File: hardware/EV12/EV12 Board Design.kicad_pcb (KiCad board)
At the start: 4 copper layers, 66 x 99.3 mm, 129 parts, among them CN2 Conn_05x02_Female, CN3 Conn_01x06_Female, CN4 Conn_01x06_Female, CN5 Conn_02x05_Male, CN6 Conn_02x05_Male, CN7 Conn_02x05_Male, J1 Conn_01x02_Socket, J10 Conn_01x08_Socket, J2 AudioJack1, J3 Conn_01x06_Socket, J9 USB_C_Receptacle, SW1 TS-1037-A11B3-D2, SW3 TS-1037-A11B3-D2, SW4 SW_Push, SW5 SW_Push, SW6 SW_SPDT, U1 STM32F405RGTx, U11 ESP32-S3-WROOM-1-N8R2, U13 BM14B(0.8)-24DS-0.4V(53), U2 BQ21040DBV, U3 CH340C, U4 USBLC6-2P6, U5 M24C02-RMN6TP, U6 WM8960CGEFL/RV, U7 TPS63060, U8 STM32F072CBTx, Y1 Crystal_GND24

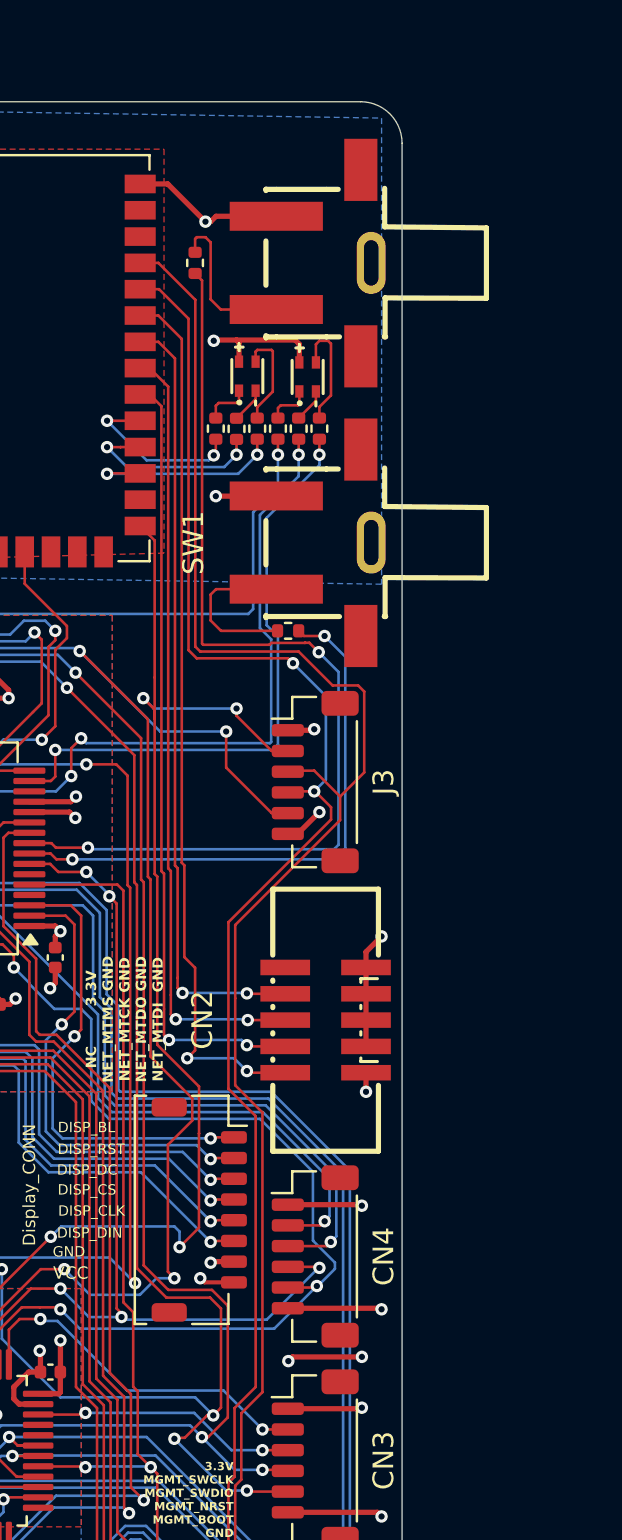
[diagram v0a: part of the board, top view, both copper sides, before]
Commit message: Replaced side buttons, switched Cap, switched to new connectors
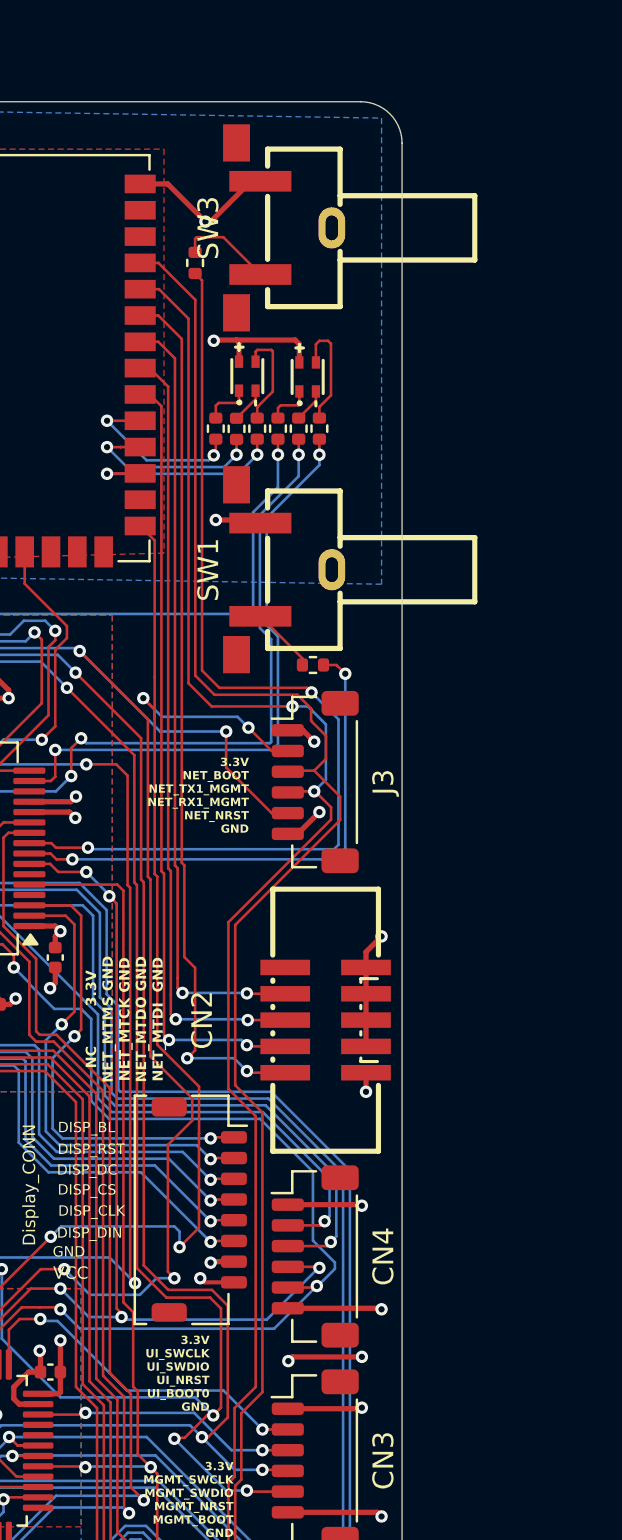
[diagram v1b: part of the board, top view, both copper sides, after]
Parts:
- SW1, SW3: footprint Hactar_Footprints:KEY-SMD_2P-L7.1-W10.6-P4.00-LS9.0 -> Hactar_Footprints:SW-SMD_L7.5-W8.0-P4.50_TS-1045-A13B3-D2
- moved SW3 2.56 mm to (174.3, 52.1)
- moved SW1 2.31 mm to (174.3, 68.6)
- moved R28 2.04 mm to (175.7, 73.2)
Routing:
- net /PTT_BTN: track 7.96 -> 3.19 mm
- net /NET_TX1_MGMT: track 100.0 -> 96.5 mm
- net /PTT_AI_BTN: track 7.66 -> 4.59 mm
- net GND: track 618.5 -> 615.7 mm
- net Net-(U1-PC0): track 27.7 -> 25.3 mm
- net Net-(U1-PC1): track 48.7 -> 48.1 mm
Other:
- board text added: "3.3V NET_BOOT NET_TX1_MGMT NET_RX1_MGMT NET_NRST GND"
- board text added: "3.3V UI_SWCLK UI_SWDIO UI_NRST UI_BOOT0 GND"

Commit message: Updated Version with fixes
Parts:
- removed SW3: TS-1037-A11B3-D2, Hactar_Footprints:SW-SMD_L7.5-W8.0-P4.50_TS-1045-A13B3-D2
- added SW2: SW_Push, Hactar_Footprints:SW-SMD_L7.5-W8.0-P4.50_TS-1045-A13B3-D2, F.Cu at (175.1, 52.1)
- SW1: value TS-1037-A11B3-D2 -> SW_Push
- moved SW1 0.75 mm to (175.1, 68.6)
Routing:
- net GND: track 615.7 -> 617.2 mm
- net /PTT_AI_BTN: track 4.59 -> 3.60 mm
